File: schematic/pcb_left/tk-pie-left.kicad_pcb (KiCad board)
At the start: 2 copper layers, 150 x 77.5 mm, 35 parts, among them IC1 PCA9539PW,118, J1 NiceView, J2 Battery Connector, U3 SN74LVC1T45DCK

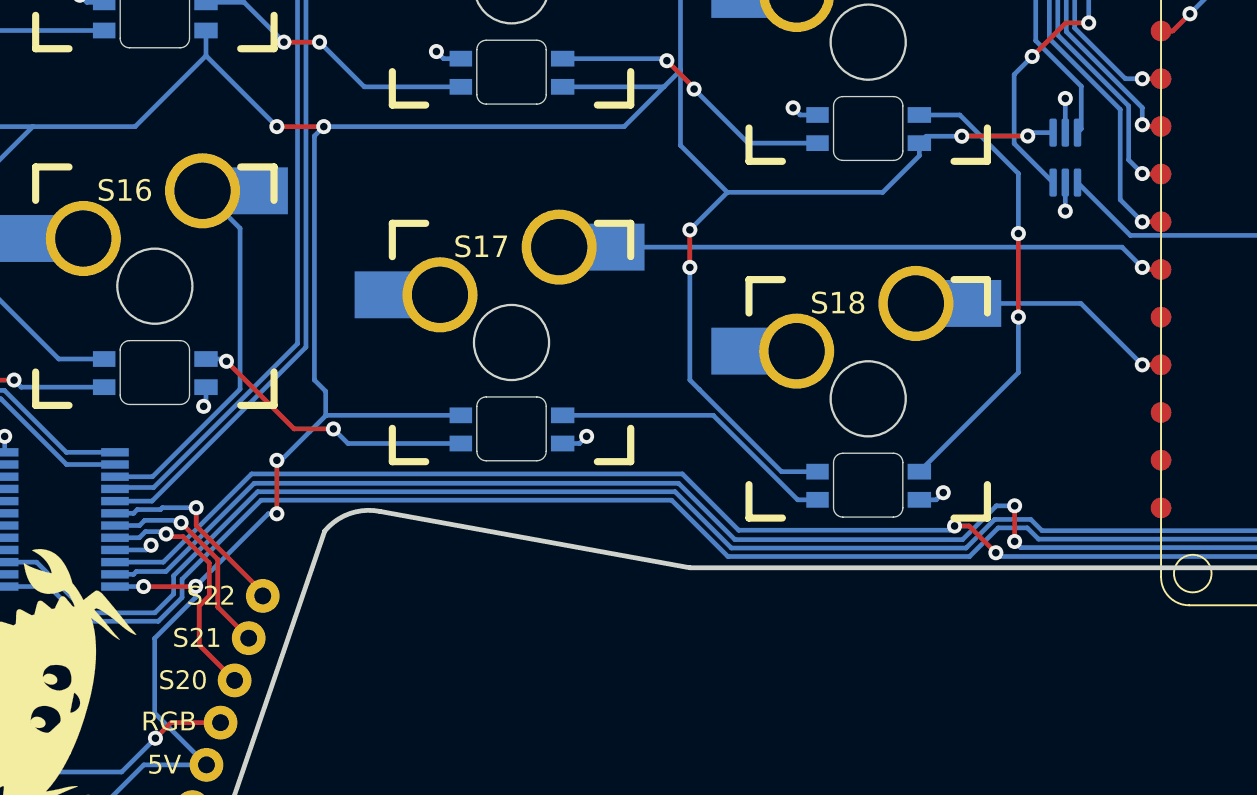
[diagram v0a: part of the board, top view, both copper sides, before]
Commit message: Move GPIO extender to 3V supply
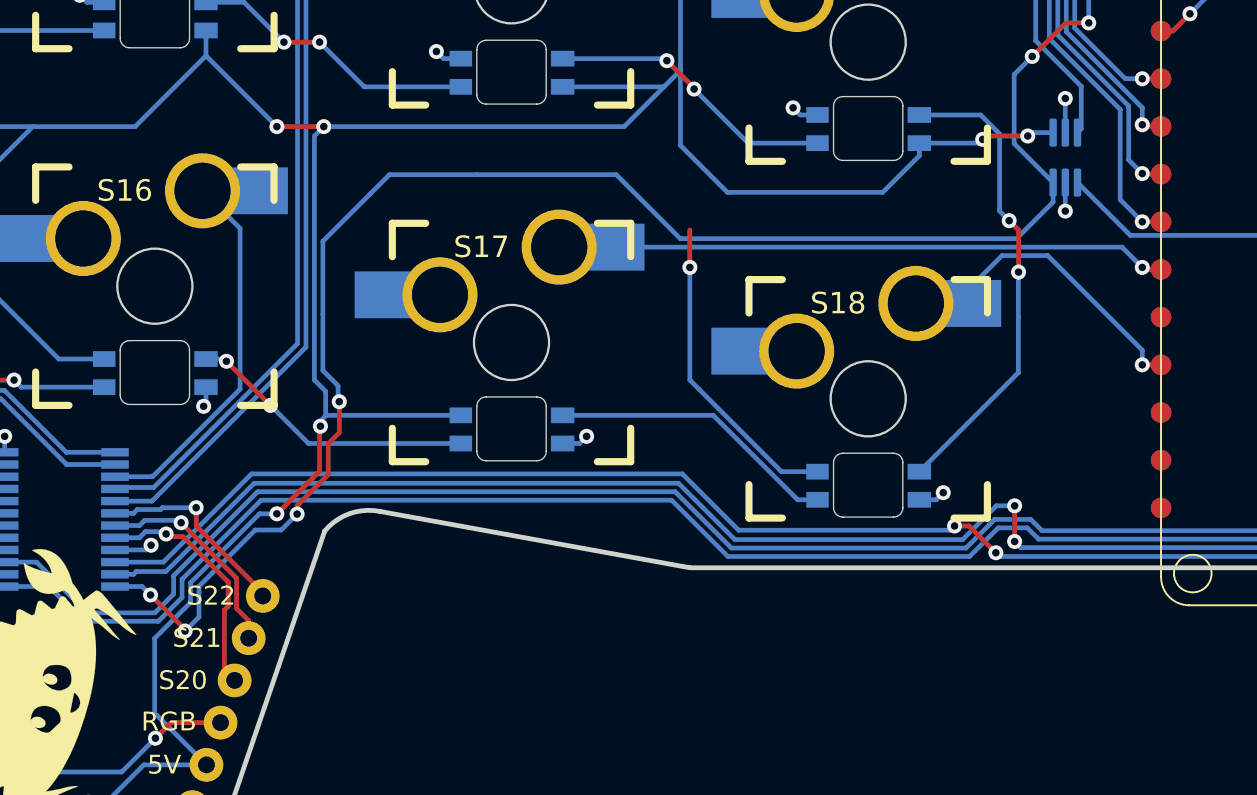
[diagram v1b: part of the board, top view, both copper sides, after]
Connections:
- IC1 pad 24: +5V -> +3.3V
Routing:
- net +3.3V: track 33.6 -> 107.4 mm, vias 5 -> 9
- net +5V: track 509.9 -> 502.9 mm, vias 34 -> 31
- net /S18: track 11.4 -> 14.5 mm
- net Net-(S12-DOUT): track 24.6 -> 25.5 mm

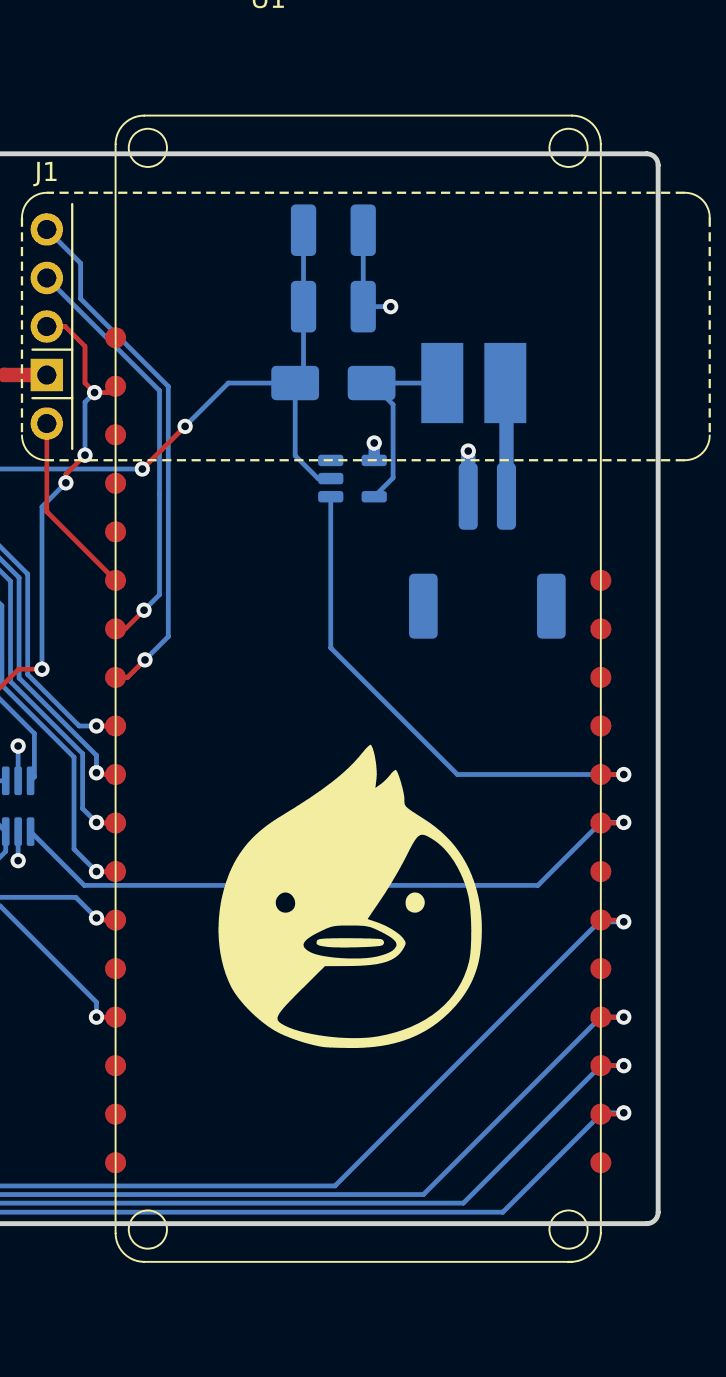
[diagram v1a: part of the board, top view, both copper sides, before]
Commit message: pcb-left: Add through-holes to vbat pads
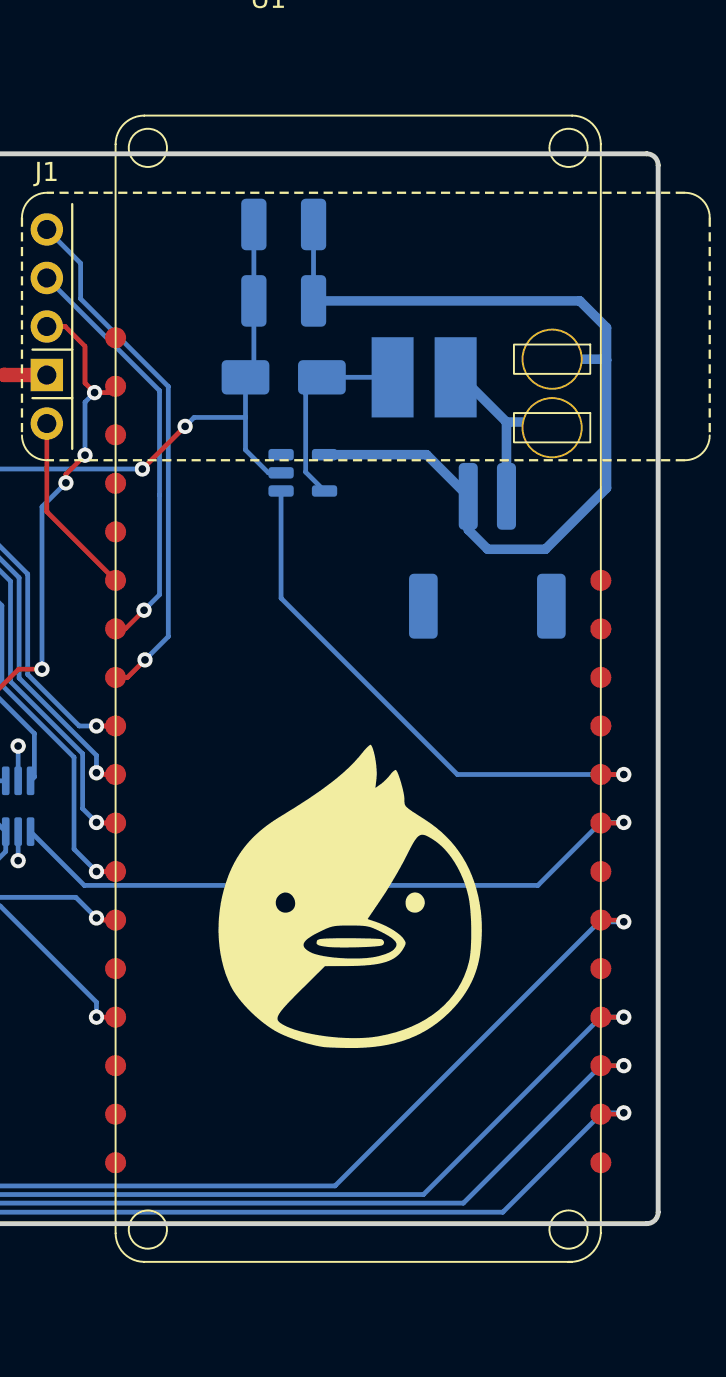
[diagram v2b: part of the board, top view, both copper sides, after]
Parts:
- moved C5 2.62 mm to (136.4, 30.7)
- moved C4 2.62 mm to (136.4, 34.7)
- moved D1 2.62 mm to (136.4, 38.7)
- moved L2 2.62 mm to (143.8, 38.7)
- moved PS1 2.62 mm to (137.4, 43.7)
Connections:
- C4 pad 2: GND -> VBAT-
- C5 pad 1: GND -> VBAT-
- J2 pad 1: /VBAT -> VBAT+
- J2 pad 2: GND -> VBAT-
- L2 pad 1: /VBAT -> VBAT+
- PS1 pad 4: GND -> VBAT-
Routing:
- net VBAT-: track 0.00 -> 50.4 mm
- net VBAT+: track 0.00 -> 11.3 mm
- net GND: track 44.3 -> 35.6 mm, vias 27 -> 24
- net /VBAT: track 5.95 -> 0.00 mm
- net +5V: track 502.9 -> 499.5 mm
- net /5V_EN: track 27.2 -> 28.6 mm

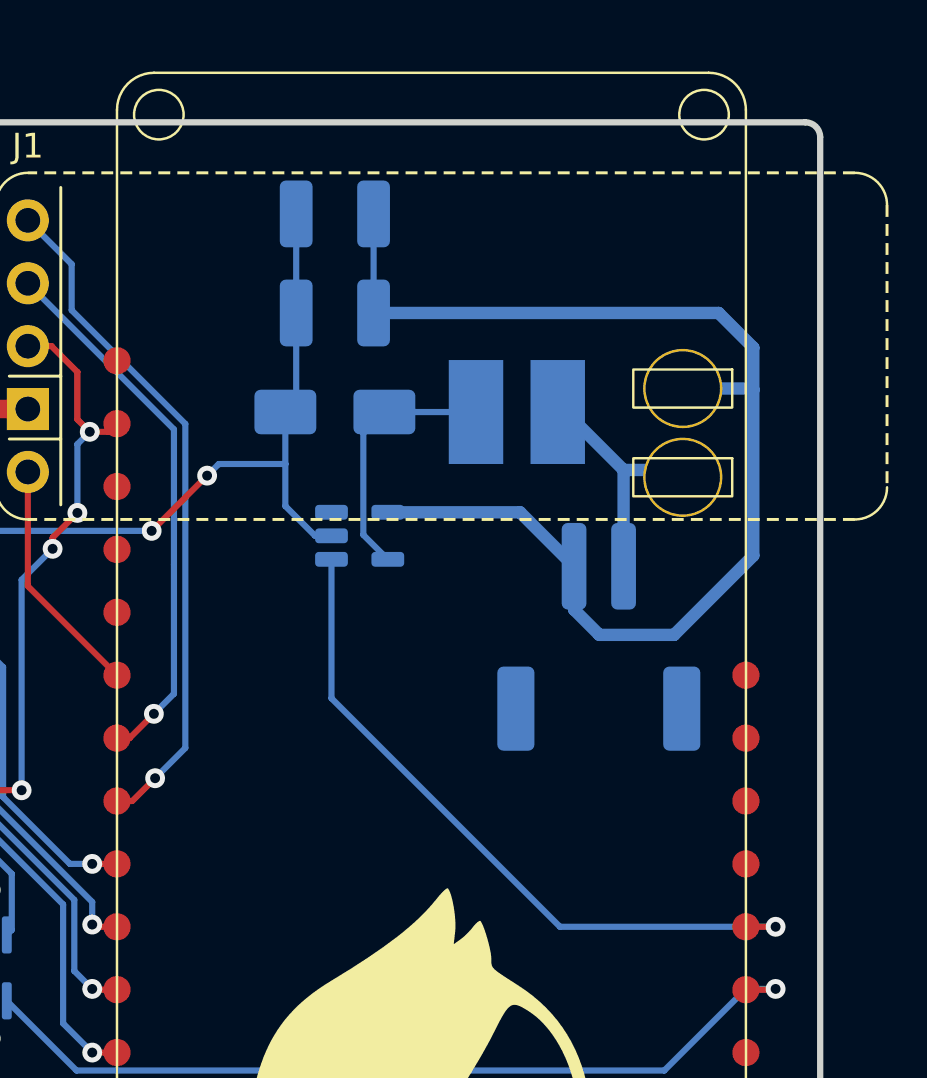
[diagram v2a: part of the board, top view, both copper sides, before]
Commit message: [W.I.P]: Added another battery connector
Also moved around our existing boost circut.
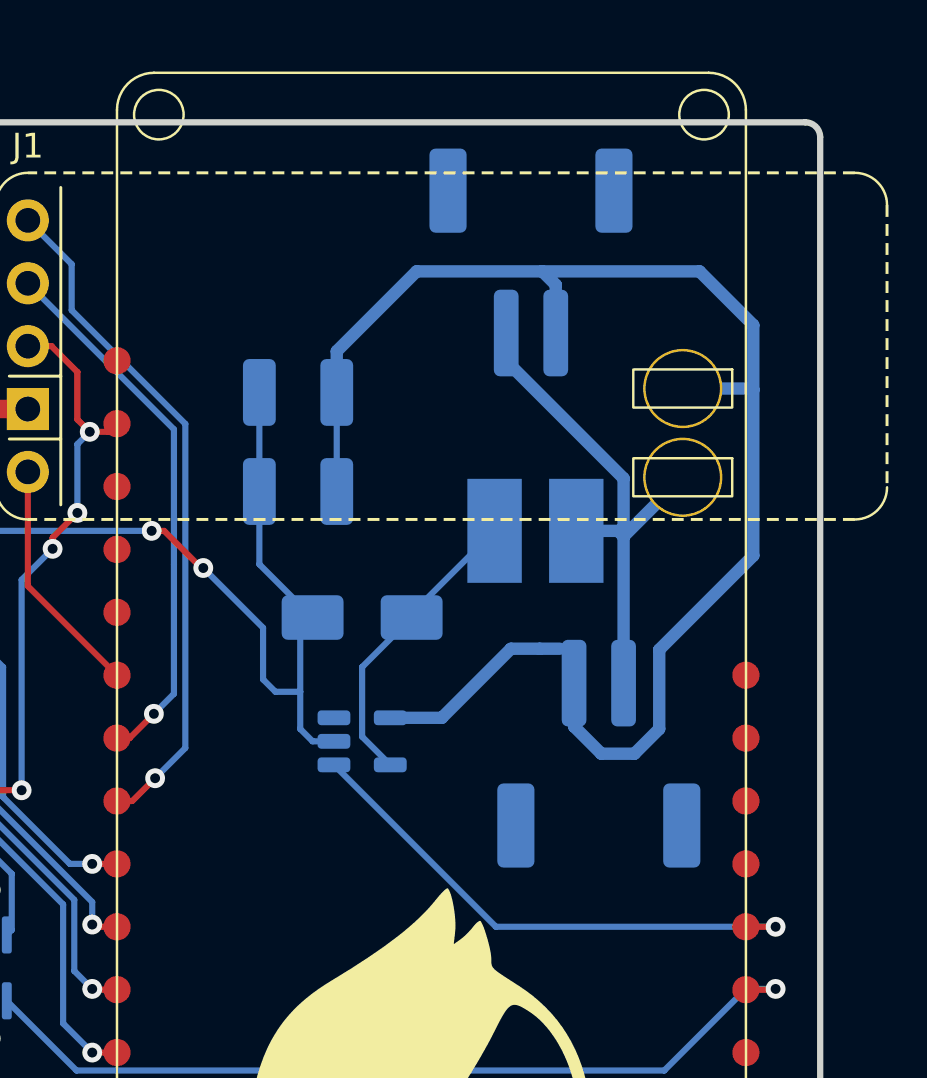
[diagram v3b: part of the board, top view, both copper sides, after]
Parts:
- added J3: Battery Connector, Connector_JST:JST_PH_S2B-PH-SM4-TB_1x02-1MP_P2.00mm_Horizontal, B.Cu at (144.3, 32.7)
- moved D1 8.37 mm to (137.5, 47.0)
- moved PS1 8.30 mm to (137.5, 52.0)
- moved C5 7.36 mm to (134.9, 37.9)
- moved C4 7.36 mm to (134.9, 41.9)
- moved L2 4.86 mm to (144.5, 43.5)
- moved J2 4.72 mm to (147.1, 52.5)
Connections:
- J2 pad 1: VBAT+ -> /VBAT
- J2 pad 2: VBAT- -> GND
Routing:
- net VBAT-: track 50.4 -> 62.3 mm
- net VBAT+: track 11.3 -> 23.2 mm
- net /5V_EN: track 28.6 -> 21.7 mm
- net +5V: track 499.5 -> 504.8 mm
- net Net-(D1-A): track 10.4 -> 12.1 mm

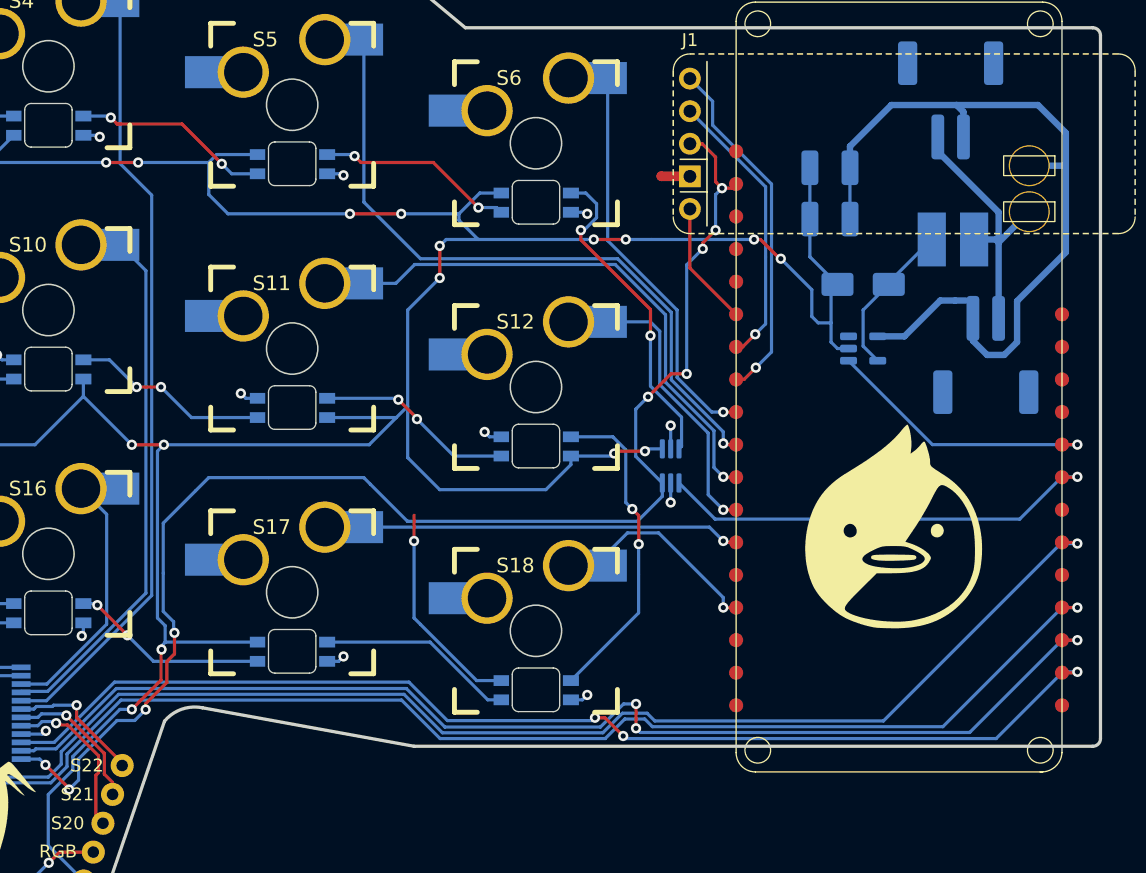
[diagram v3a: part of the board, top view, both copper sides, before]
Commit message: Slight updates to battery circuits
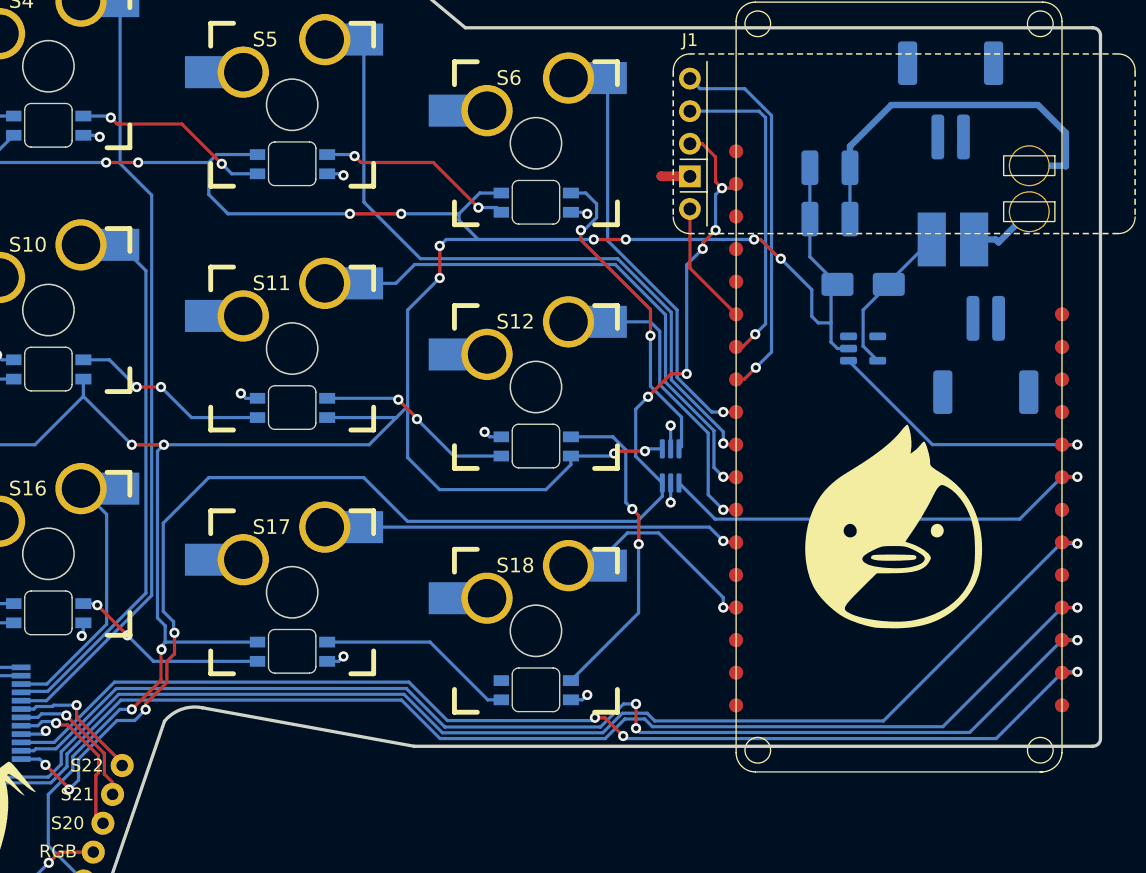
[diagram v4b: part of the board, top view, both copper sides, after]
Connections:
- J3 pad 1: VBAT+ -> /VBAT
- J3 pad 2: VBAT- -> GND
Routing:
- net VBAT-: track 62.3 -> 30.2 mm
- net VBAT+: track 23.2 -> 5.38 mm
- net +5V: track 504.8 -> 488.0 mm, vias 31 -> 30
- net /NV_SCK: track 22.1 -> 25.2 mm
- net /NV_MOSI: track 27.6 -> 29.6 mm
